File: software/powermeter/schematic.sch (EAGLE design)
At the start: 24 parts, among them J1 AVR_SPI_PRG_6NS, U1 LCD-16X2SILK, Y1 16MHz

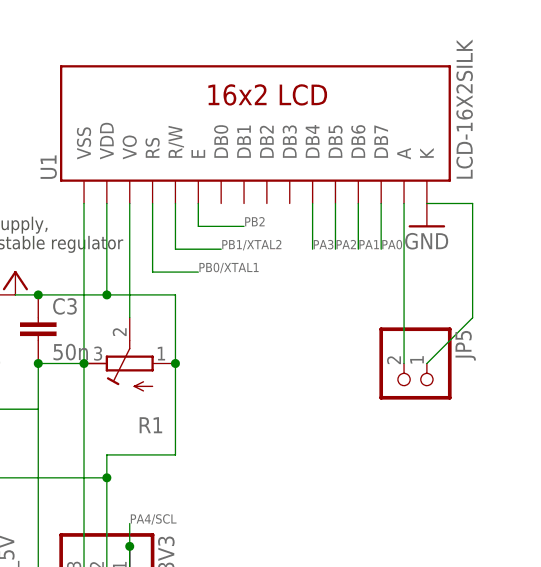
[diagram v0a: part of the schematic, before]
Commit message: the backlight needs resistor afterall, it just is a very small one when compared to led resistors in general
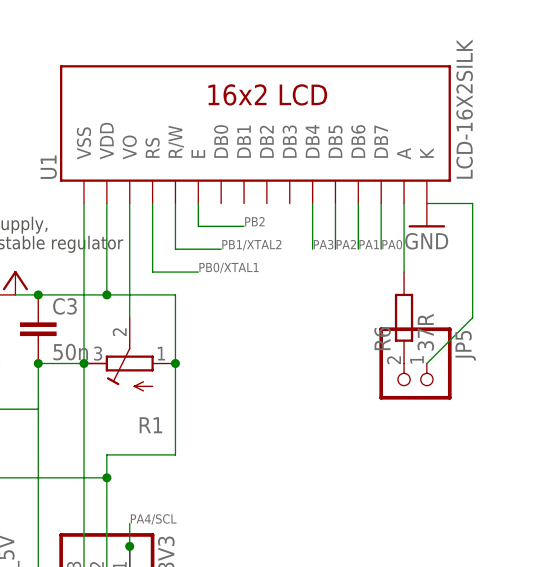
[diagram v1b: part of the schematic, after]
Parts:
- added R6: 37R, resistor:R-EU_0204/7
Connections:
- removed net LCD_BL_A: JP5.2, U1.A
- new net N$1: JP5.2, R6.1
- new net N$3: R6.2, U1.A
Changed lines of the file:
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@@
 <part name="GND8" library="supply1" deviceset="GND" device=""/>
 <part name="JP5" library="pinhead" deviceset="PINHD-1X2" device=""/>
+<part name="R6" library="resistor" deviceset="R-EU_" device="0204/7" value="37R"/>
 </parts>
 <sheets>
@@
 <instance part="GND8" gate="1" x="231.14" y="114.3"/>
 <instance part="JP5" gate="G$1" x="228.6" y="96.52" rot="R270"/>
+<instance part="R6" gate="G$1" x="228.6" y="104.14" rot="R90"/>
 </instances>
 <busses>
@@
 </segment>
 </net>
-<net name="LCD_BL_A" class="0">
-<segment>
+<net name="N$1" class="0">
+<segment>
+<pinref part="JP5" gate="G$1" pin="2"/>
+<pinref part="R6" gate="G$1" pin="1"/>
+</segment>
+</net>
+<net name="N$3" class="0">
+<segment>
+<pinref part="R6" gate="G$1" pin="2"/>
 <pinref part="U1" gate="G$1" pin="A"/>
-<pinref part="JP5" gate="G$1" pin="2"/>
-<wire x1="228.6" y1="116.84" x2="228.6" y2="99.06" width="0.1524" layer="91"/>
-</segment>
-</net>
+<wire x1="228.6" y1="109.22" x2="228.6" y2="116.84" width="0.1524" layer="91"/>
+</segment>
+</net>
